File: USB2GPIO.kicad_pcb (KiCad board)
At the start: 2 copper layers, 41.5 x 35 mm, 44 parts, among them J1 Conn_01x04, J7 Conn_01x03, J8 Conn_01x03, J9 Conn_01x02, Q1 S8050, U10 PCF8574T, U11 HX9193, U12 SL2.1S, U2 CH340E, U3 CH340E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

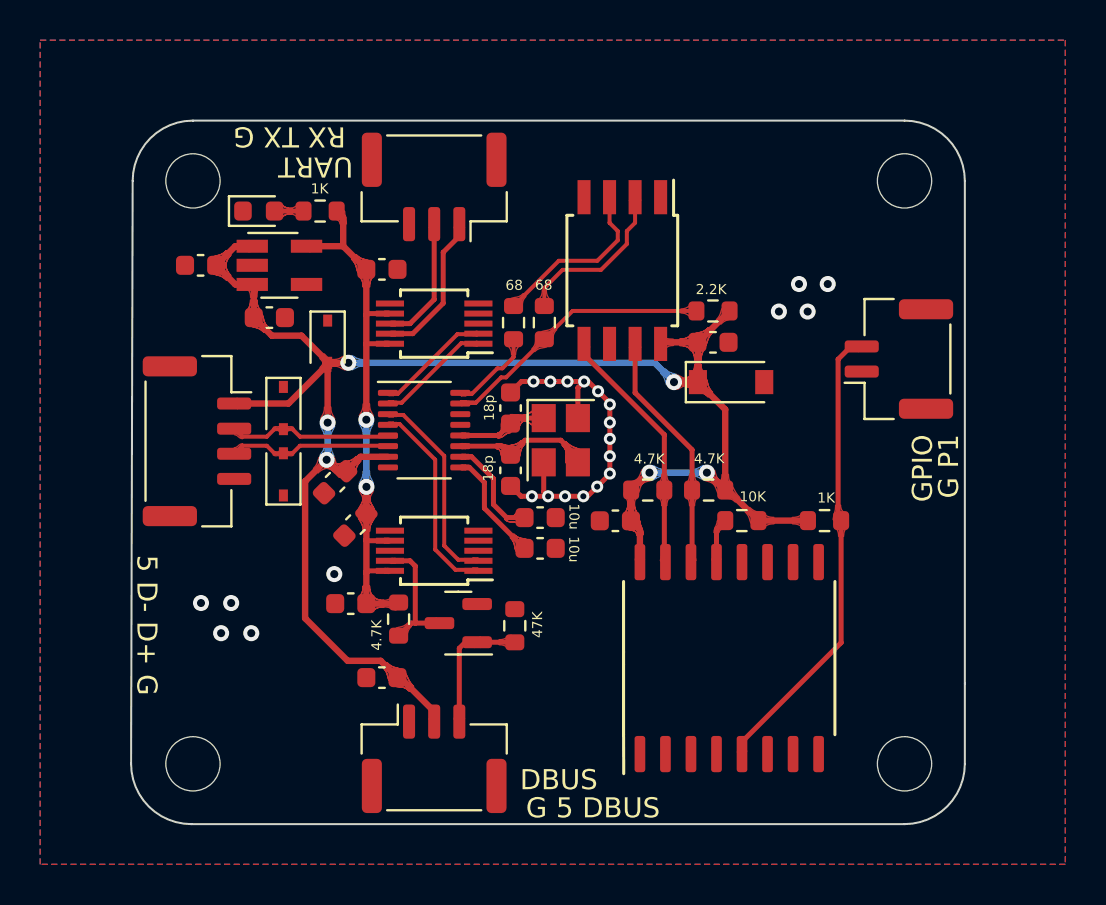
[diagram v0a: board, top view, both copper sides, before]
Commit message: Add ESD protection
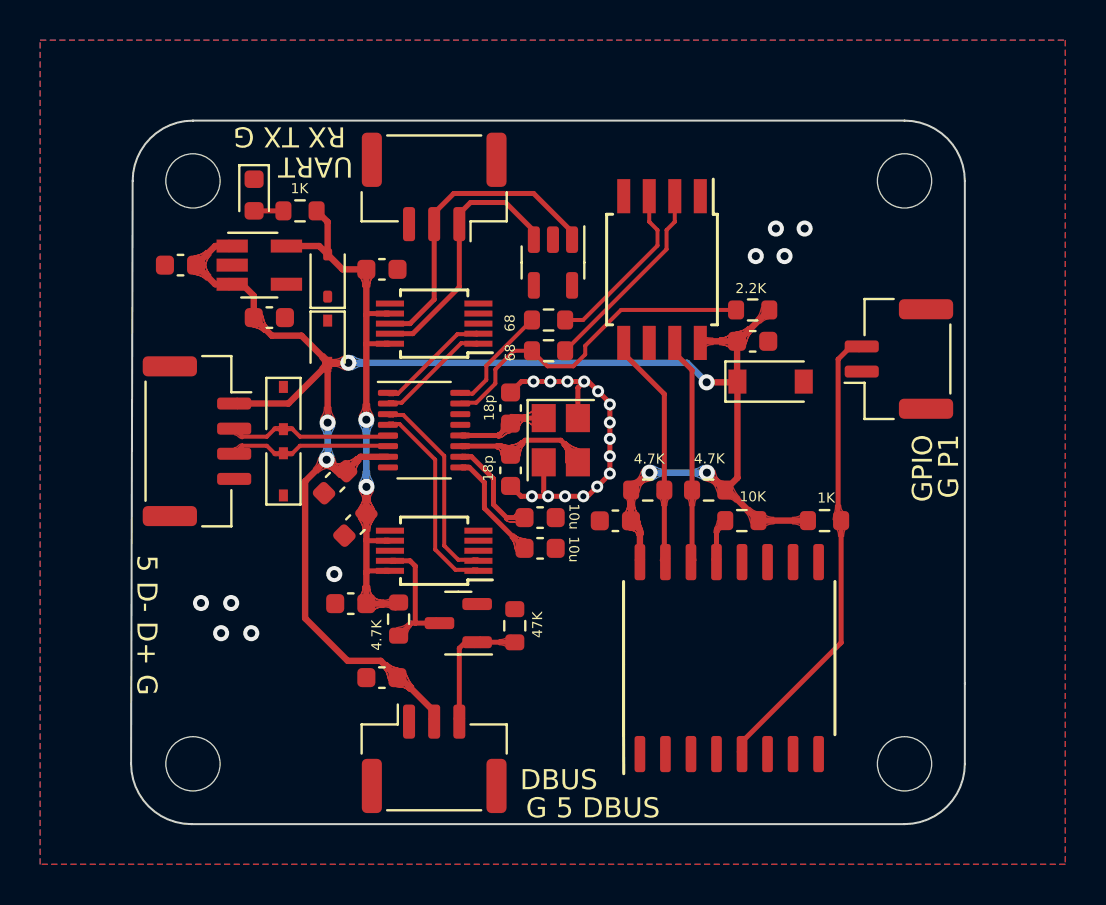
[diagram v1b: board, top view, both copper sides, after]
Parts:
- added D1: BV05C, Diode_SMD:D_SOD-323, F.Cu at (47.3, 58.7)
- added U1: ~, Package_TO_SOT_SMD:SOT-23-5, F.Cu at (58.5, 58.1)
- moved U9 1.98 mm to (63.9, 58.4)
- moved C31 1.98 mm to (68.4, 62.0)
- moved R18 1.98 mm to (68.4, 60.4)
- moved D13 1.97 mm to (69.3, 64.0)
- moved R20 1.74 mm to (58.3, 60.9), turned to 180 degrees
- moved R19 1.42 mm to (58.3, 62.5), turned to 180 degrees
- moved C28 1.00 mm to (40.0, 58.2)
- moved U11 1.00 mm to (43.9, 58.2)
- moved R14 1.00 mm to (45.9, 55.5)
- moved D9 0.83 mm to (43.6, 54.7), turned to -90 degrees
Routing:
- net /UART/TXD: track 6.45 -> 15.4 mm
- net /UART/RXD: track 7.54 -> 13.0 mm
- net /GPIO/D-: track 14.3 -> 17.0 mm
- net +5V: track 86.9 -> 89.5 mm
- net /GPIO/*D-: track 8.41 -> 9.95 mm
- net /3V3: track 28.3 -> 29.9 mm
- net /GPIO/SDA: track 12.5 -> 11.8 mm
- net /GPIO/SCL: track 12.1 -> 11.3 mm
- net /GPIO/D+: track 4.76 -> 5.51 mm

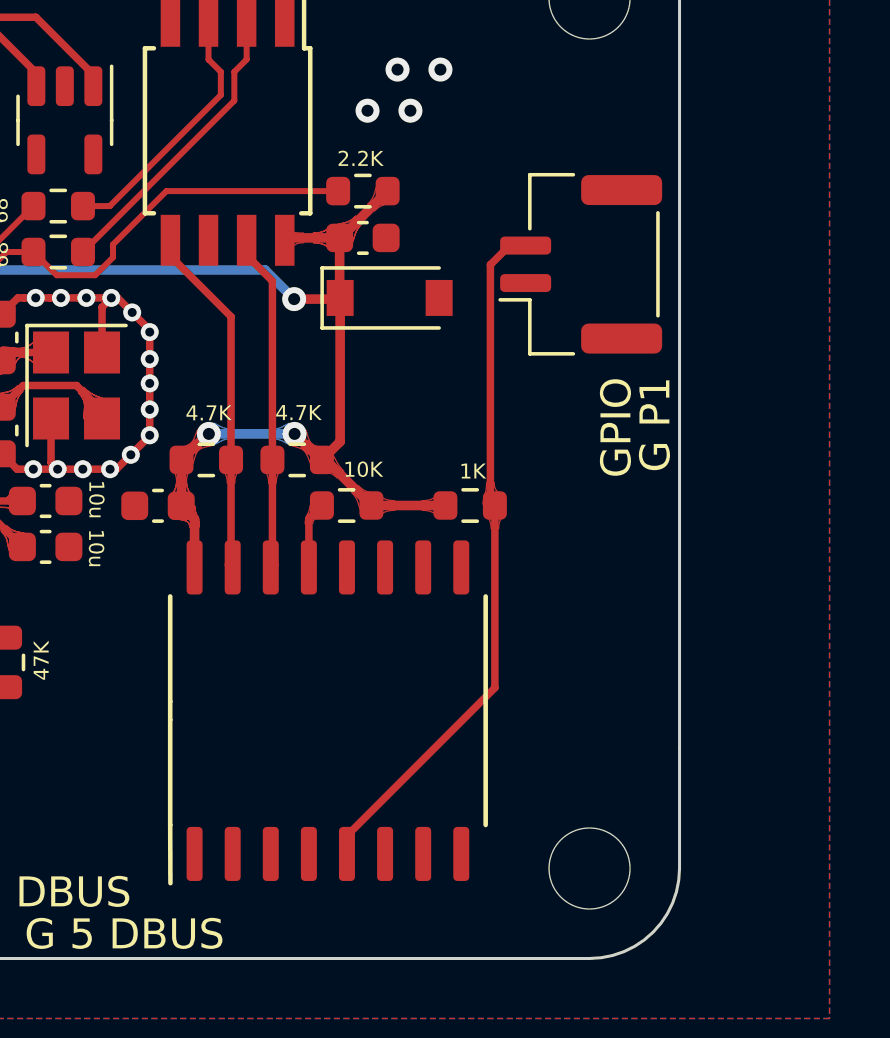
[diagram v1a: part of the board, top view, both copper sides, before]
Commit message: Return to PNP-out
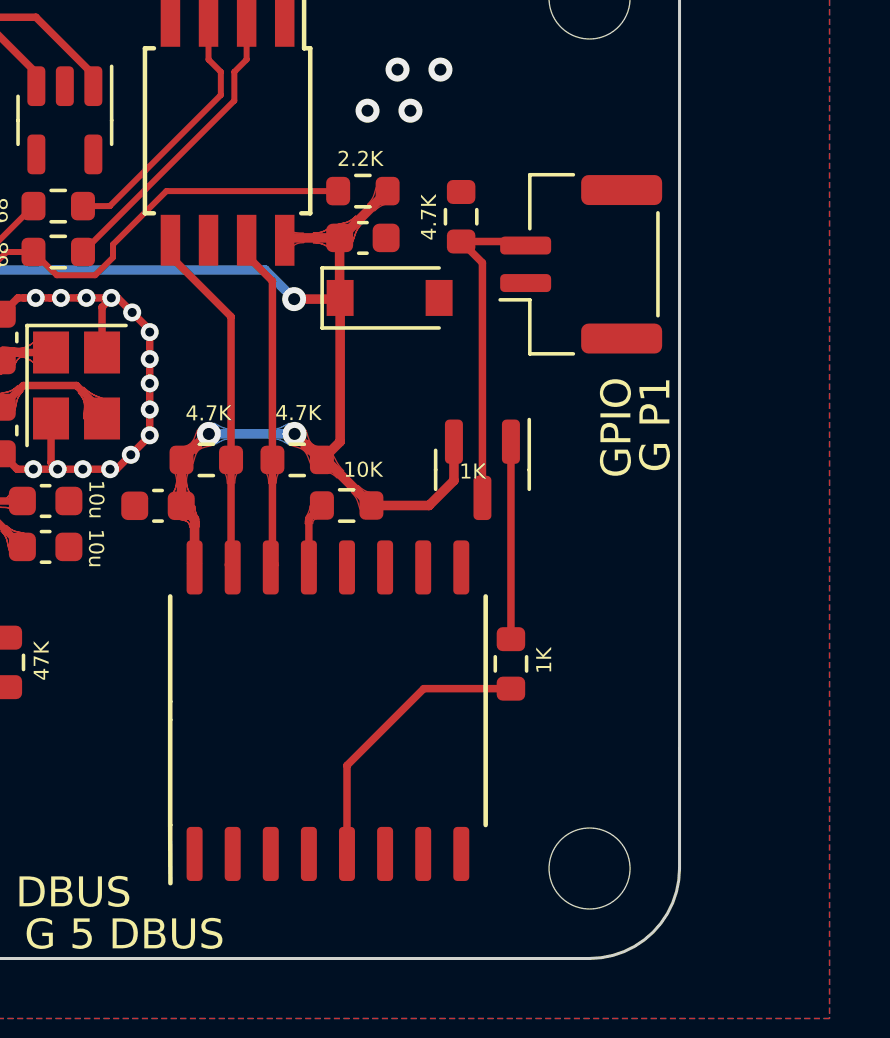
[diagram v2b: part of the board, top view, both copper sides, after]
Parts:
- removed R30: 1K, Resistor_SMD:R_0603_1608Metric
- added Q2: Q_PNP_BEC, Package_TO_SOT_SMD:SOT-23, F.Cu at (72.4, 69.7)
- added R1: 1K, Resistor_SMD:R_0603_1608Metric, F.Cu at (73.4, 76.2)
- added R4: 4.7K, Resistor_SMD:R_0603_1608Metric, F.Cu at (71.7, 61.3)
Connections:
- U10 pad 5: /GPIO/P1 -> Net-(U10-P1)
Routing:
- net /GPIO/P1: track 23.2 -> 11.0 mm
- net Net-(U10-P1): track 0.00 -> 9.48 mm
- net Net-(Q2-B): track 0.00 -> 6.58 mm
- net +5V: track 89.5 -> 91.4 mm
